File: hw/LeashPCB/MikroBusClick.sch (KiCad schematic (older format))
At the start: 2 parts, among them J701 mikroBUS, J702 mikroBUS

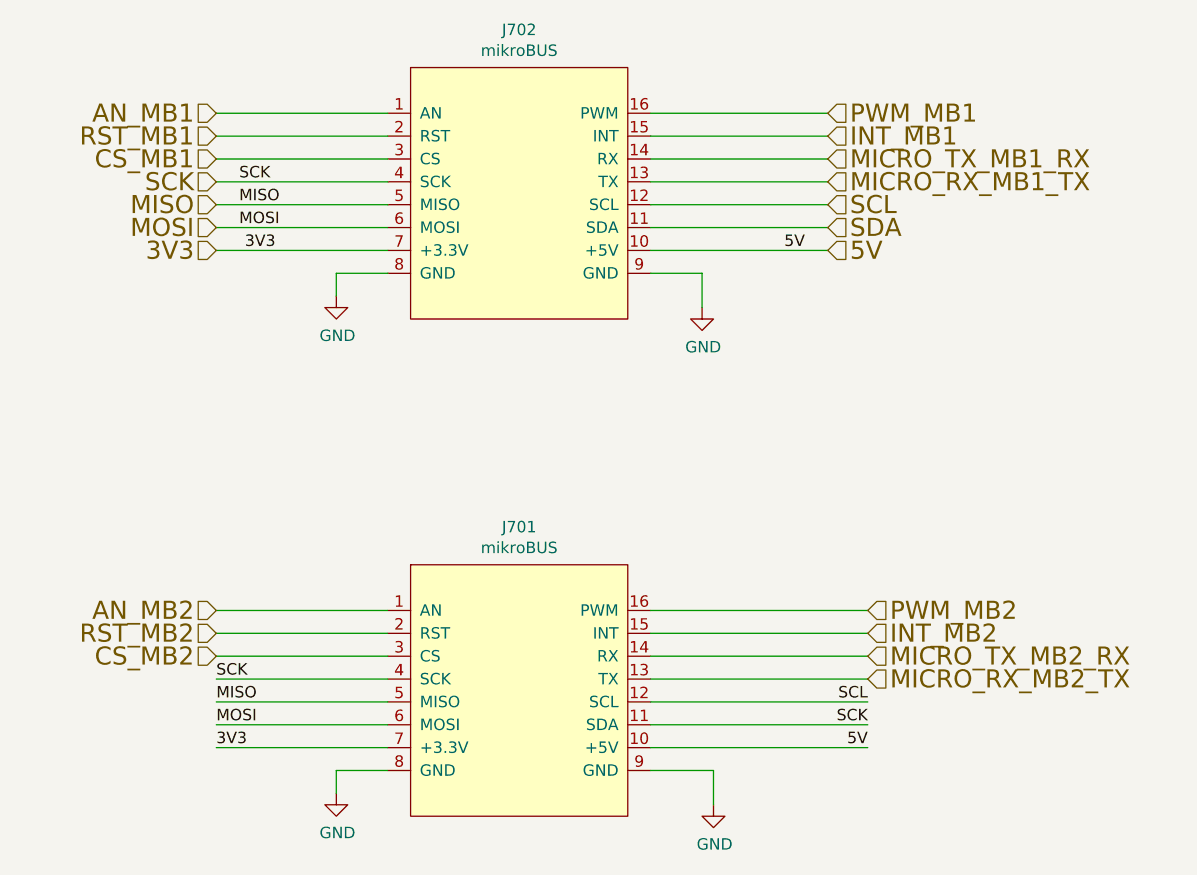
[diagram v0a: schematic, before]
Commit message: Swapped out USB and antenna sections and refactored outline, started routing
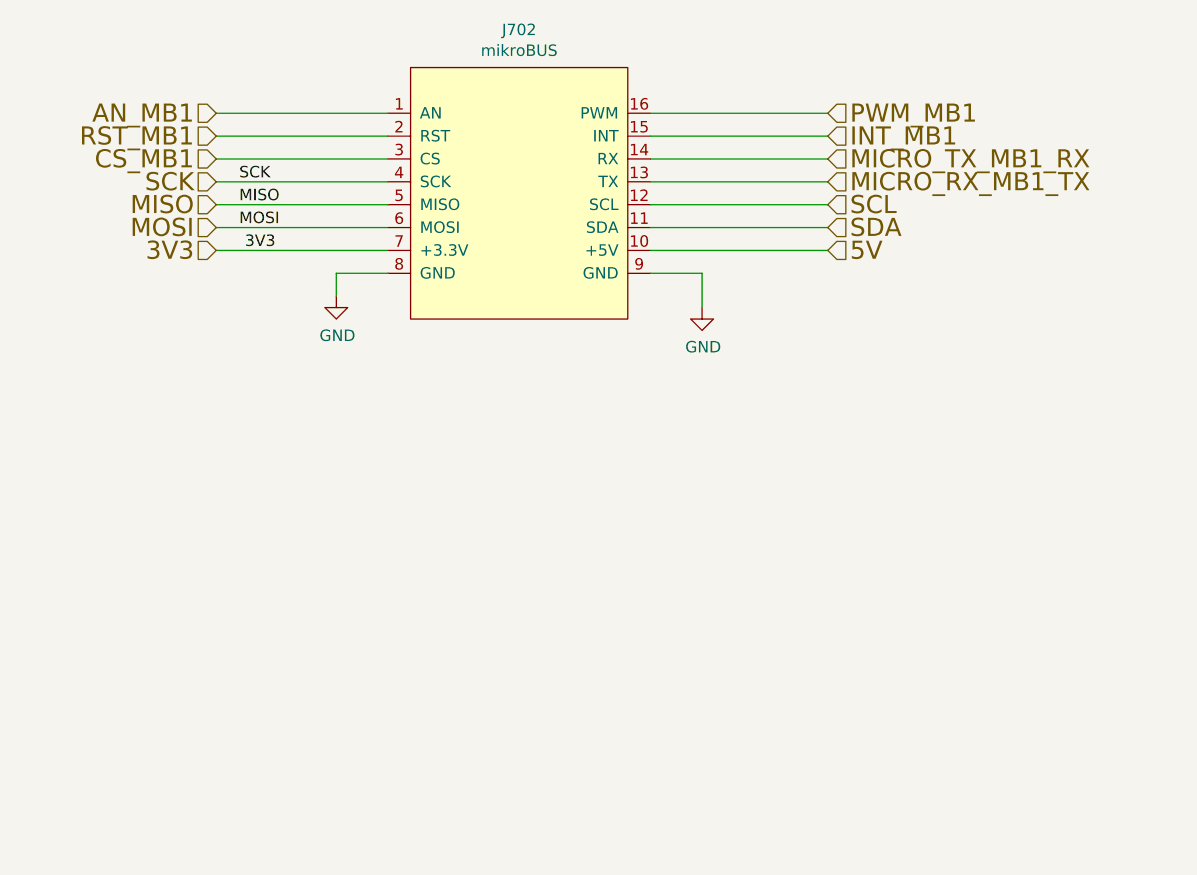
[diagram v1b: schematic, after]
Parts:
- removed J701: mikroBUS, leash:MikroBus-SMD, symbol LeashPCB:mikroBUS
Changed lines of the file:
@@
 EESchema Schematic File Version 4
-LIBS:LeashPCB-cache
 EELAYER 30 0
 EELAYER END
 $Descr B 17000 11000
 encoding utf-8
-Sheet 9 10
+Sheet 8 9
 Title "BeagleDust Leash PCB"
 Date "2019-08-12"
@@
 	1    0    0    -1
 $EndComp
-$Comp
-L LeashPCB:mikroBUS J?
-U 1 1 5D092DA2
-P 8675 6200
-AR Path="/5D092DA2" Ref="J?"  Part="1"
-AR Path="/5D066680/5D092DA2" Ref="J701"  Part="1"
-F 0 "J701" H 8700 6915 50  0000 C CNN
-F 1 "mikroBUS" H 8700 6824 50  0000 C CNN
-F 2 "leash:MikroBus-SMD" H 8475 6400 50  0001 C CNN
-F 3 "" H 8475 6400 50  0001 C CNN
-F 4 "0" H 8675 6200 50  0001 C CNN "Standard Price"
-F 5 "N/A" H 8675 6200 50  0001 C CNN "Description"
-F 6 "https://www.digikey.com/product-detail/en/sullins-connector-solutions/NPTC081KFXC-RC/S5600-ND/776058" H 8675 6200 50  0001 C CNN "Link1"
-F 7 "NPTC081KFXC-RC" H 8675 6200 50  0001 C CNN "MPN1"
-F 8 "" H 8675 6200 50  0001 C CNN "Population"
-F 9 "Sullins" H 8675 6200 50  0001 C CNN "Vendor1"
-F 10 "CONN HDR 8POS 0.1 TIN SMD" H 8675 6200 50  0001 C CNN "Short Description"
-	1    8675 6200
-	1    0    0    -1
-$EndComp
 Text HLabel 7375 4275 0    79   Input ~ 0
 3V3
@@
 Text HLabel 7375 3875 0    79   Input ~ 0
 CS_MB1
-Text HLabel 7375 6050 0    79   Input ~ 0
-CS_MB2
 Text HLabel 7375 3975 0    79   Input ~ 0
 SCK
@@
 Text HLabel 10050 3675 2    79   Input ~ 0
 PWM_MB1
-Text HLabel 10225 5850 2    79   Input ~ 0
-PWM_MB2
 Text HLabel 10050 3775 2    79   Input ~ 0
 INT_MB1
-Text HLabel 10225 5950 2    79   Input ~ 0
-INT_MB2
 Text HLabel 10050 3875 2    79   Input ~ 0
 MICRO_TX_MB1_RX
-Text HLabel 10225 6050 2    79   Input ~ 0
-MICRO_TX_MB2_RX
 Text HLabel 10050 3975 2    79   Input ~ 0
 MICRO_RX_MB1_TX
-Text HLabel 10225 6150 2    79   Input ~ 0
-MICRO_RX_MB2_TX
 Text HLabel 10050 4175 2    79   Input ~ 0
 SDA
@@
 Wire Wire Line
 	10050 4175 9275 4175
-Wire Wire Line
-	8125 6050 7375 6050
-Wire Wire Line
-	7375 5850 8125 5850
-Text HLabel 7375 5850 0    79   Input ~ 0
-AN_MB2
-Wire Wire Line
-	7375 5950 8125 5950
 Text Label 7475 3975 0    50   ~ 0
 SCK
@@
 Text Label 7500 4275 0    50   ~ 0
 3V3
-Wire Wire Line
-	8125 6450 7375 6450
-Wire Wire Line
-	7375 6350 8125 6350
-Wire Wire Line
-	7375 6250 8125 6250
-Wire Wire Line
-	7375 6150 8125 6150
-Text Label 7375 6150 0    50   ~ 0
-SCK
-Text Label 7375 6250 0    50   ~ 0
-MISO
-Text Label 7375 6350 0    50   ~ 0
-MOSI
-Text Label 7375 6450 0    50   ~ 0
-3V3
-Wire Wire Line
-	8125 6550 7900 6550
-Wire Wire Line
-	7900 6550 7900 6650
-$Comp
-L power:GND #PWR0106
-U 1 1 5D217A46
-P 7900 6650
-F 0 "#PWR0106" H 7900 6400 50  0001 C CNN
-F 1 "GND" H 7905 6477 50  0000 C CNN
-F 2 "" H 7900 6650 50  0001 C CNN
-F 3 "" H 7900 6650 50  0001 C CNN
-	1    7900 6650
-	1    0    0    -1
-$EndComp
-Wire Wire Line
-	9275 5850 10225 5850
-Wire Wire Line
-	10225 5950 9275 5950
-Wire Wire Line
-	9275 6050 10225 6050
-Wire Wire Line
-	10225 6150 9275 6150
-Wire Wire Line
-	9275 6250 10225 6250
-Wire Wire Line
-	9275 6350 10225 6350
-Wire Wire Line
-	9275 6450 10225 6450
-$Comp
-L power:GND #PWR0107
-U 1 1 5D220EE5
-P 9550 6700
-F 0 "#PWR0107" H 9550 6450 50  0001 C CNN
-F 1 "GND" H 9555 6527 50  0000 C CNN
-F 2 "" H 9550 6700 50  0001 C CNN
-F 3 "" H 9550 6700 50  0001 C CNN
-	1    9550 6700
-	1    0    0    -1
-$EndComp
-Wire Wire Line
-	9550 6550 9550 6700
-Wire Wire Line
-	9275 6550 9550 6550
-Text Label 10225 6250 2    50   ~ 0
-SCL
-Text Label 10225 6350 2    50   ~ 0
-SCK
-Text Label 10225 6450 2    50   ~ 0
-5V
-Text Label 9950 4275 2    50   ~ 0
-5V
-Text HLabel 7375 5950 0    79   Input ~ 0
-RST_MB2
 $EndSCHEMATC

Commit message: Added a the second header back in and started hooking it up. Swapped DIO12/13 and 21/22 pins to get the correct UART configuration
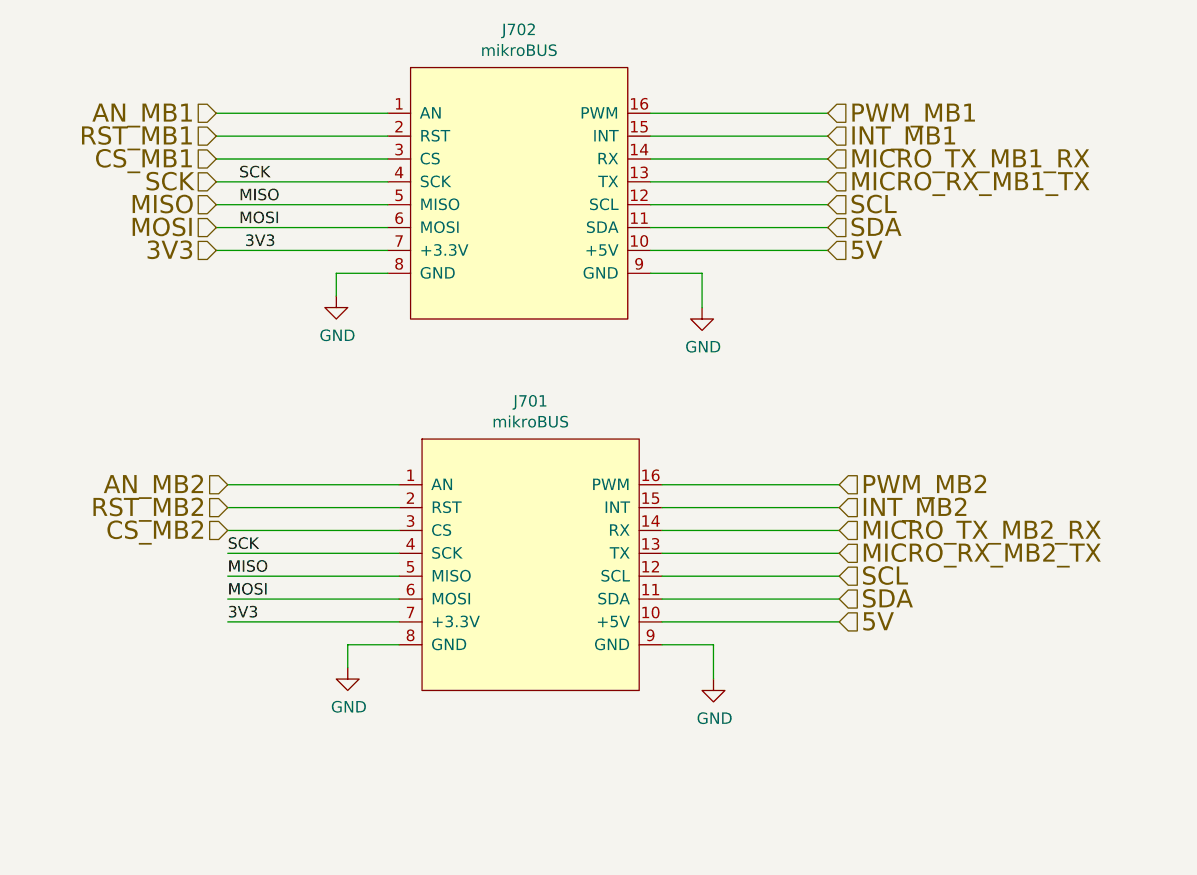
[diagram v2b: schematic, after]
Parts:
- added J701: mikroBUS, leash:MikroBus-SMD, symbol LeashPCB:mikroBUS
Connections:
- net 3V3: now also J701.7 (+3.3V)
- net 5V: now also J701.10 (+5V)
- net GND: now also J701.8 (GND), J701.9 (GND)
- net MISO: now also J701.5 (MISO)
- net MOSI: now also J701.6 (MOSI)
- net SCK: now also J701.4 (SCK)
- net SCL: now also J701.12 (SCL)
- net SDA: now also J701.11 (SDA)
- new net AN_MB2: J701.1 (AN)
- new net CS_MB2: J701.3 (CS)
- new net INT_MB2: J701.15 (INT)
- new net MICRO_RX_MB2_TX: J701.13 (TX)
- new net MICRO_TX_MB2_RX: J701.14 (RX)
- new net PWM_MB2: J701.16 (PWM)
- new net RST_MB2: J701.2 (RST)
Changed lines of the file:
@@
 $Descr B 17000 11000
 encoding utf-8
-Sheet 8 9
+Sheet 7 9
 Title "BeagleDust Leash PCB"
 Date "2019-08-12"
@@
 Text Label 7500 4275 0    50   ~ 0
 3V3
+$Comp
+L LeashPCB:mikroBUS J?
+U 1 1 5E8910E4
+P 8725 5650
+AR Path="/5E8910E4" Ref="J?"  Part="1"
+AR Path="/5D066680/5E8910E4" Ref="J701"  Part="1"
+F 0 "J701" H 8750 6365 50  0000 C CNN
+F 1 "mikroBUS" H 8750 6274 50  0000 C CNN
+F 2 "leash:MikroBus-SMD" H 8525 5850 50  0001 C CNN
+F 3 "" H 8525 5850 50  0001 C CNN
+F 4 "0" H 8725 5650 50  0001 C CNN "Standard Price"
+F 5 "N/A" H 8725 5650 50  0001 C CNN "Description"
+F 6 "https://www.digikey.com/product-detail/en/sullins-connector-solutions/NPTC081KFXC-RC/S5600-ND/776058" H 8725 5650 50  0001 C CNN "Link1"
+F 7 "NPTC081KFXC-RC" H 8725 5650 50  0001 C CNN "MPN1"
+F 8 "Sullins" H 8725 5650 50  0001 C CNN "Vendor1"
+F 9 "CONN HDR 8POS 0.1 TIN SMD" H 8725 5650 50  0001 C CNN "Short Description"
+	1    8725 5650
+	1    0    0    -1
+$EndComp
+Text HLabel 10100 5900 2    79   Input ~ 0
+5V
+Text HLabel 7425 5300 0    79   Input ~ 0
+AN_MB2
+Text HLabel 7425 5400 0    79   Input ~ 0
+RST_MB2
+Text HLabel 7425 5500 0    79   Input ~ 0
+CS_MB2
+Text HLabel 10100 5300 2    79   Input ~ 0
+PWM_MB2
+Text HLabel 10100 5400 2    79   Input ~ 0
+INT_MB2
+Text HLabel 10100 5500 2    79   Input ~ 0
+MICRO_TX_MB2_RX
+Text HLabel 10100 5600 2    79   Input ~ 0
+MICRO_RX_MB2_TX
+Text HLabel 10100 5800 2    79   Input ~ 0
+SDA
+Wire Wire Line
+	8175 5900 7425 5900
+Wire Wire Line
+	8175 6000 7950 6000
+Wire Wire Line
+	7950 6000 7950 6100
+$Comp
+L power:GND #PWR0103
+U 1 1 5E8910FE
+P 7950 6100
+F 0 "#PWR0103" H 7950 5850 50  0001 C CNN
+F 1 "GND" H 7955 5927 50  0000 C CNN
+F 2 "" H 7950 6100 50  0001 C CNN
+F 3 "" H 7950 6100 50  0001 C CNN
+	1    7950 6100
+	1    0    0    -1
+$EndComp
+Wire Wire Line
+	7425 5800 8175 5800
+Wire Wire Line
+	7425 5700 8175 5700
+Wire Wire Line
+	7425 5600 8175 5600
+Wire Wire Line
+	7425 5300 8175 5300
+Wire Wire Line
+	8175 5400 7425 5400
+Wire Wire Line
+	8175 5500 7425 5500
+Wire Wire Line
+	9325 5900 10100 5900
+$Comp
+L power:GND #PWR0120
+U 1 1 5E89110F
+P 9550 6150
+F 0 "#PWR0120" H 9550 5900 50  0001 C CNN
+F 1 "GND" H 9555 5977 50  0000 C CNN
+F 2 "" H 9550 6150 50  0001 C CNN
+F 3 "" H 9550 6150 50  0001 C CNN
+	1    9550 6150
+	1    0    0    -1
+$EndComp
+Wire Wire Line
+	9550 6000 9325 6000
+Wire Wire Line
+	9550 6000 9550 6150
+Text HLabel 10100 5700 2    79   Input ~ 0
+SCL
+Wire Wire Line
+	10100 5300 9325 5300
+Wire Wire Line
+	10100 5400 9325 5400
+Wire Wire Line
+	9325 5500 10100 5500
+Wire Wire Line
+	10100 5600 9325 5600
+Wire Wire Line
+	9325 5700 10100 5700
+Wire Wire Line
+	10100 5800 9325 5800
+Text Label 7425 5600 0    50   ~ 0
+SCK
+Text Label 7425 5700 0    50   ~ 0
+MISO
+Text Label 7425 5800 0    50   ~ 0
+MOSI
+Text Label 7425 5900 0    50   ~ 0
+3V3
 $EndSCHEMATC

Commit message: Migrated all hierarchical labels to global labels
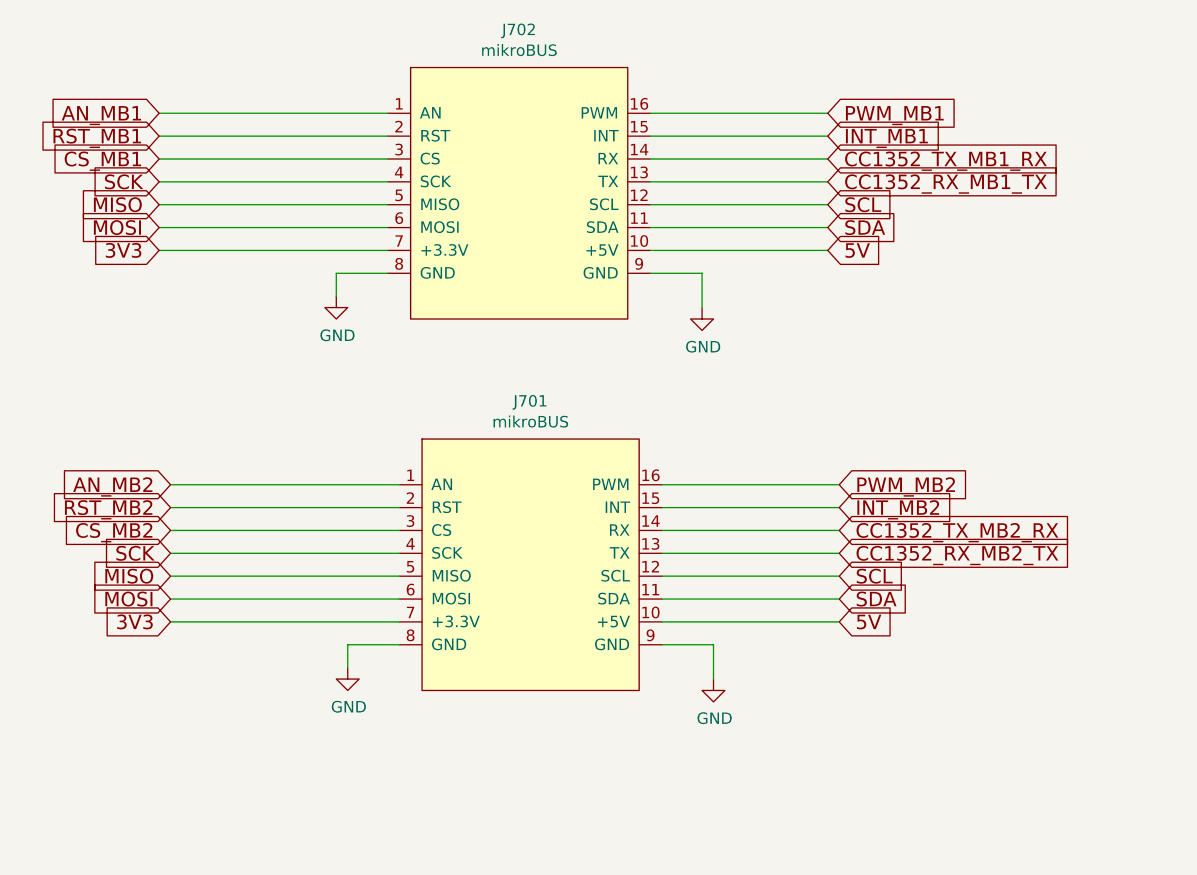
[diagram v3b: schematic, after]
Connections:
- net MICRO_RX_MB1_TX renamed CC1352_RX_MB1_TX
- net MICRO_RX_MB2_TX renamed CC1352_RX_MB2_TX
- net MICRO_TX_MB1_RX renamed CC1352_TX_MB1_RX
- net MICRO_TX_MB2_RX renamed CC1352_TX_MB2_RX
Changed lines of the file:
@@
 	1    0    0    -1
 $EndComp
-Text HLabel 7375 4275 0    79   Input ~ 0
-3V3
-Text HLabel 10050 4275 2    79   Input ~ 0
-5V
-Text HLabel 7375 3675 0    79   Input ~ 0
-AN_MB1
-Text HLabel 7375 3775 0    79   Input ~ 0
-RST_MB1
-Text HLabel 7375 3875 0    79   Input ~ 0
-CS_MB1
-Text HLabel 7375 3975 0    79   Input ~ 0
-SCK
-Text HLabel 7375 4075 0    79   Input ~ 0
-MISO
-Text HLabel 7375 4175 0    79   Input ~ 0
-MOSI
-Text HLabel 10050 3675 2    79   Input ~ 0
-PWM_MB1
-Text HLabel 10050 3775 2    79   Input ~ 0
-INT_MB1
-Text HLabel 10050 3875 2    79   Input ~ 0
-MICRO_TX_MB1_RX
-Text HLabel 10050 3975 2    79   Input ~ 0
-MICRO_RX_MB1_TX
-Text HLabel 10050 4175 2    79   Input ~ 0
-SDA
-Wire Wire Line
-	8125 4275 7375 4275
 Wire Wire Line
 	8125 4375 7900 4375
@@
 	1    0    0    -1
 $EndComp
-Wire Wire Line
-	7375 4175 8125 4175
-Wire Wire Line
-	7375 4075 8125 4075
-Wire Wire Line
-	7375 3975 8125 3975
-Wire Wire Line
-	7375 3675 8125 3675
-Wire Wire Line
-	8125 3775 7375 3775
-Wire Wire Line
-	8125 3875 7375 3875
 Wire Wire Line
 	9275 4275 10050 4275
@@
 Wire Wire Line
 	9500 4375 9500 4525
-Text HLabel 10050 4075 2    79   Input ~ 0
-SCL
 Wire Wire Line
 	10050 3675 9275 3675
@@
 Wire Wire Line
 	10050 4175 9275 4175
-Text Label 7475 3975 0    50   ~ 0
-SCK
-Text Label 7475 4075 0    50   ~ 0
-MISO
-Text Label 7475 4175 0    50   ~ 0
-MOSI
-Text Label 7500 4275 0    50   ~ 0
-3V3
 $Comp
 L LeashPCB:mikroBUS J?
@@
 	1    0    0    -1
 $EndComp
-Text HLabel 10100 5900 2    79   Input ~ 0
-5V
-Text HLabel 7425 5300 0    79   Input ~ 0
-AN_MB2
-Text HLabel 7425 5400 0    79   Input ~ 0
-RST_MB2
-Text HLabel 7425 5500 0    79   Input ~ 0
-CS_MB2
-Text HLabel 10100 5300 2    79   Input ~ 0
-PWM_MB2
-Text HLabel 10100 5400 2    79   Input ~ 0
-INT_MB2
-Text HLabel 10100 5500 2    79   Input ~ 0
-MICRO_TX_MB2_RX
-Text HLabel 10100 5600 2    79   Input ~ 0
-MICRO_RX_MB2_TX
-Text HLabel 10100 5800 2    79   Input ~ 0
-SDA
-Wire Wire Line
-	8175 5900 7425 5900
 Wire Wire Line
 	8175 6000 7950 6000
@@
 	1    0    0    -1
 $EndComp
-Wire Wire Line
-	7425 5800 8175 5800
-Wire Wire Line
-	7425 5700 8175 5700
-Wire Wire Line
-	7425 5600 8175 5600
-Wire Wire Line
-	7425 5300 8175 5300
-Wire Wire Line
-	8175 5400 7425 5400
-Wire Wire Line
-	8175 5500 7425 5500
-Wire Wire Line
-	9325 5900 10100 5900
 $Comp
 L power:GND #PWR0120
@@
 Wire Wire Line
 	9550 6000 9550 6150
-Text HLabel 10100 5700 2    79   Input ~ 0
+Text GLabel 7125 3675 0    63   Input ~ 0
+AN_MB1
+Text GLabel 7125 3775 0    63   Input ~ 0
+RST_MB1
+Text GLabel 7125 3875 0    63   Input ~ 0
+CS_MB1
+Wire Wire Line
+	7125 3675 8125 3675
+Wire Wire Line
+	7125 3775 8125 3775
+Wire Wire Line
+	7125 3875 8125 3875
+Text GLabel 7125 3975 0    63   Input ~ 0
+SCK
+Text GLabel 7125 4075 0    63   Input ~ 0
+MISO
+Text GLabel 7125 4175 0    63   Input ~ 0
+MOSI
+Text GLabel 7125 4275 0    63   Input ~ 0
+3V3
+Wire Wire Line
+	7125 3975 8125 3975
+Wire Wire Line
+	8125 4075 7125 4075
+Wire Wire Line
+	7125 4175 8125 4175
+Wire Wire Line
+	8125 4275 7125 4275
+Text GLabel 10050 3675 2    63   Input ~ 0
+PWM_MB1
+Text GLabel 10050 3775 2    63   Input ~ 0
+INT_MB1
+Text GLabel 10050 3875 2    63   Input ~ 0
+CC1352_TX_MB1_RX
+Text GLabel 10050 3975 2    63   Input ~ 0
+CC1352_RX_MB1_TX
+Text GLabel 10050 4075 2    63   Input ~ 0
 SCL
+Text GLabel 10050 4175 2    63   Input ~ 0
+SDA
+Text GLabel 10050 4275 2    63   Input ~ 0
+5V
+Wire Wire Line
+	9325 5900 10100 5900
 Wire Wire Line
 	10100 5300 9325 5300
@@
 Wire Wire Line
 	10100 5800 9325 5800
-Text Label 7425 5600 0    50   ~ 0
+Text GLabel 10100 5300 2    63   Input ~ 0
+PWM_MB2
+Text GLabel 10100 5400 2    63   Input ~ 0
+INT_MB2
+Text GLabel 10100 5500 2    63   Input ~ 0
+CC1352_TX_MB2_RX
+Text GLabel 10100 5600 2    63   Input ~ 0
+CC1352_RX_MB2_TX
+Text GLabel 10100 5700 2    63   Input ~ 0
+SCL
+Text GLabel 10100 5800 2    63   Input ~ 0
+SDA
+Text GLabel 10100 5900 2    63   Input ~ 0
+5V
+Text GLabel 7175 5300 0    63   Input ~ 0
+AN_MB2
+Text GLabel 7175 5400 0    63   Input ~ 0
+RST_MB2
+Text GLabel 7175 5500 0    63   Input ~ 0
+CS_MB2
+Wire Wire Line
+	7175 5300 8175 5300
+Wire Wire Line
+	7175 5400 8175 5400
+Wire Wire Line
+	7175 5500 8175 5500
+Text GLabel 7175 5600 0    63   Input ~ 0
 SCK
-Text Label 7425 5700 0    50   ~ 0
+Text GLabel 7175 5700 0    63   Input ~ 0
 MISO
-Text Label 7425 5800 0    50   ~ 0
+Text GLabel 7175 5800 0    63   Input ~ 0
 MOSI
-Text Label 7425 5900 0    50   ~ 0
+Text GLabel 7175 5900 0    63   Input ~ 0
 3V3
+Wire Wire Line
+	7175 5600 8175 5600
+Wire Wire Line
+	8175 5700 7175 5700
+Wire Wire Line
+	7175 5800 8175 5800
+Wire Wire Line
+	8175 5900 7175 5900
 $EndSCHEMATC
